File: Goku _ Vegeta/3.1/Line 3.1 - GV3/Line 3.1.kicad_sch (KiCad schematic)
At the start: 112 parts, among them J1 Solenoid, J10 RIGHT HEADERS, J11 Kicker Voltmeter, J3 Motor 1, J4 Motor 3, J5 Motor 2, J6 Motor 4, J7 BATTERY POWER, J8 I2C TO MASTER, J9 LEFT HEADERS, Q2 BSC040N10NS5, U1 LM2587S-ADJ, U10 TPS62132, U11 TPS62133, U2 TB67H420FTG Dual/Single Motor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, U3 TB67H420FTG Dual/Single Motor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, U4 TB67H420FTG Dual/Single Motor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, U5 TB67H420FTG Dual/Single Motor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, U7 NXV55UNR, U9 DEV-16771

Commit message: abt halfway done with line 3.0
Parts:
- removed J3: Motor 1, Connector_PinSocket_2.54mm:PinSocket_1x06_P2.54mm_Vertical, symbol Connector:Conn_01x06_Pin
- removed J4: Motor 3, Connector_PinSocket_2.54mm:PinSocket_1x06_P2.54mm_Vertical, symbol Connector:Conn_01x06_Pin
- removed J5: Motor 2, Connector_PinSocket_2.54mm:PinSocket_1x06_P2.54mm_Vertical, symbol Connector:Conn_01x06_Pin
- removed J6: Motor 4, Connector_PinSocket_2.54mm:PinSocket_1x06_P2.54mm_Vertical, symbol Connector:Conn_01x06_Pin
- removed U2, U3, U4, U5: TB67H420FTG Dual/Single Motor Driver Carrier, TB67H420FTG Dual_Single Motor Driver Carrier:TB67H420FTG DualSingle Motor Driver Carrier, symbol TB67H420FTG Dual_Single Motor Driver Carrier:LM2587S-ADJ
- added A17, A18, A19, A20, A21, A22, A23, A24, A25, A26, A27, A28, A29, A30, A31, A32, A33, A34, A35, A36: ALS-PT19-315C/L177/TR8, ALS-PT19-315C_L177_TR8:XDCR_ALS-PT19-315C_L177_TR8, symbol ALS-PT19-315C_L177_TR8:ALS-PT19-315C/L177/TR8
- added LED17, LED18, LED19, LED20, LED21, LED22, LED23, LED24, LED25, LED26, LED27, LED28, LED29, LED30, LED31, LED32, LED33, LED34, LED35, LED36: JB2835AWT-W-U30GA0000-N0000001, JB2835AWT-W-U30GA0000-N0000001:LED_J2835_CRW, symbol JB2835AWT-W-U30GA0000-N0000001:JB2835AWT-W-U30GA0000-N0000001
- added R40, R42, R44, R46, R48, R50, R52, R54, R56, R58, R60, R62, R64, R66, R68, R70, R72, R74, R76, R78: 12R, Resistor_SMD:R_0805_2012Metric, symbol Device:R_Small_US
- added R41, R43, R45, R47, R49, R51, R53, R55, R57, R59, R61, R63, R65, R67, R69, R71, R73, R75, R77, R79: 10K, Resistor_SMD:R_0805_2012Metric, symbol Device:R_Small_US
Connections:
- net SEN1 is gone; now on net 14: A1.2, A10.2, A11.2, A12.2, A13.2, A14.2, A15.2, A16.2, A2.2, A3.2, A4.2, A5.2, A6.2, A7.2, A8.2, A9.2, R10.2, R12.2, R14.2, R16.2, R18.2, R20.2, R22.2, R24.2, R26.2, R28.2, R33.2, R35.2, R37.2, R39.2, R5.2, R8.2
- net +3V3: now also A17.1, A18.1, A19.1, A20.1, A21.1, A22.1, A23.1, A24.1, A25.1, A26.1, A27.1, A28.1, A29.1, A30.1, A31.1, A32.1, A33.1, A34.1, A35.1, A36.1, R40.1, R42.1, R44.1, R46.1, R48.1, R50.1, R52.1, R54.1, R56.1, R58.1, R60.1, R62.1, R64.1, R66.1, R68.1, R70.1, R72.1, R74.1, R76.1, R78.1
- net 14: now also A17.2, A18.2, A19.2, A20.2, A21.2, A22.2, A23.2, A24.2, A25.2, A26.2, A27.2, A28.2, A29.2, A30.2, A31.2, A32.2, A33.2, A34.2, A35.2, A36.2, R41.2, R43.2, R45.2, R47.2, R49.2, R51.2, R53.2, R55.2, R57.2, R59.2, R61.2, R63.2, R65.2, R67.2, R69.2, R71.2, R73.2, R75.2, R77.2, R79.2; no longer J9.18 (Pin_18), U9.26 (A12)
- net 15: no longer J9.19 (Pin_19), U9.27 (A13)
- net GND: now also R41.1, R43.1, R45.1, R47.1, R49.1, R51.1, R53.1, R55.1, R57.1, R59.1, R61.1, R63.1, R65.1, R67.1, R69.1, R71.1, R73.1, R75.1, R77.1, R79.1
- net MSFTDRN: now also LED17.1, LED18.1, LED19.1, LED20.1, LED21.1, LED22.1, LED23.1, LED24.1, LED25.1, LED26.1, LED27.1, LED28.1, LED29.1, LED30.1, LED31.1, LED32.1, LED33.1, LED34.1, LED35.1, LED36.1
- new net: LED28.2, R62.2
- new net: LED31.2, R68.2
- new net: LED26.2, R58.2
- new net: LED24.2, R54.2
- new net: LED34.2, R74.2
- new net: LED22.2, R50.2
- new net: LED21.2, R48.2
- new net: LED18.2, R42.2
- new net: LED19.2, R44.2
- new net: LED32.2, R70.2
- new net: LED27.2, R60.2
- new net: LED17.2, R40.2
- new net: LED25.2, R56.2
- new net: LED20.2, R46.2
- new net: LED36.2, R78.2
- new net: LED33.2, R72.2
- new net: LED30.2, R66.2
- new net: LED23.2, R52.2
- new net: LED35.2, R76.2
- new net: LED29.2, R64.2
- new net 26: J9.18 (Pin_18), U9.26 (A12)
- new net 27: J9.19 (Pin_19), U9.27 (A13)
- no-connect marks 54 -> 14
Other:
- note added: "Cross line sensors - conditional poll 1"
- note added: "DONE 16 outer circle line sensors DONE 16 cross sensors DONE 8 inner cicle sensors DONE 36 line sensors in total maxon brushless motor controllers adapter board two cables connecting line and main pcb - power xt60 cable - idc data cable kicker charge pump no imu 36 leds using actual LED driver good power rails that are rated for 2 x of projected power draw"
- note added: "GOALS FOR LINE 3.1"
- note added: "Inner ring line sensors - conditional poll 2"
- note added: "Outer ring line sensors - constant poll"
- note added: "STILL GOTTA CHAT WITH KEVIN ABOUT LINE SENSOR ORENTATION - WE ARE NO ONLY DOES 16 LINE SENSORS IN TOTOAL THAT ALL ME HAVE GOT TO WORK WITH"
- note removed: "2nd Warning Line Sensors - Conditonal Poll"
- note removed: "Urgent Line Sensors - Conditional Poll"
- note removed: "Warning Line Sensors - Constant Poll"
- moved on the sheet: A1, A2, A3, A4, C1, C10, C15, C16, C17, C18, C2, C3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

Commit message: move to 3.1
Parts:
- removed A17, A18, A19, A20, A21, A22, A23, A24, A25, A26, A27, A28, A29, A30, A31, A32, A33, A34, A35, A36: ALS-PT19-315C/L177/TR8, ALS-PT19-315C_L177_TR8:XDCR_ALS-PT19-315C_L177_TR8, symbol ALS-PT19-315C_L177_TR8:ALS-PT19-315C/L177/TR8
- removed C1, C6: 100uF, Capacitor_THT:CP_Radial_D10.0mm_P5.00mm, symbol Device:C_Polarized_Small
- removed C10, C16: 0.1uF, Capacitor_SMD:C_0805_2012Metric, symbol Device:C_Polarized_Small
- removed C15, C8: 10uF, Capacitor_SMD:C_0805_2012Metric, symbol Device:C_Polarized_Small
- removed C17, C9: 3.3nF, Capacitor_SMD:C_0805_2012Metric, symbol Device:C_Polarized_Small
- removed C18, C7: 22uF, Capacitor_SMD:C_0805_2012Metric, symbol Device:C_Polarized_Small
- removed C2, C5: 1uF, Capacitor_SMD:C_0805_2012Metric, symbol Device:C_Polarized_Small
- removed C3, C4: 560uF, Capacitor_THT:CP_Radial_D18.0mm_P7.50mm, symbol Device:C_Polarized
- removed D1: SS510, Diode_SMD:D_SOD-128, symbol Device:D_Schottky
- removed D2, D3, D5: STTH2002G-TR, Package_TO_SOT_SMD:TO-263-2, symbol Diode:STTH2002G
- removed J1: Solenoid, TerminalBlock:TerminalBlock_bornier-2_P5.08mm, symbol Connector:Screw_Terminal_01x02
- removed J11: Kicker Voltmeter, TerminalBlock:TerminalBlock_bornier-2_P5.08mm, symbol Connector:Screw_Terminal_01x02
- removed J7: BATTERY POWER, Connector_AMASS:AMASS_XT60-F_1x02_P7.20mm_Vertical, symbol Connector:Conn_01x02_Male
- removed J8: I2C TO MASTER, Connector_JST:JST_XH_B4B-XH-AM_1x04_P2.50mm_Vertical, symbol Connector:Conn_01x04_Male
- removed L1: 56uH, Inductor_SMD:L_Bourns_SRR1260, symbol Device:L
- removed L2, L3: 2.2uH, Inductor_SMD:L_Bourns_SRR1260, symbol Device:L
- removed LED17, LED18, LED19, LED20, LED21, LED22, LED23, LED24, LED25, LED26, LED27, LED28, LED29, LED30, LED31, LED32, LED33, LED34, LED35, LED36: JB2835AWT-W-U30GA0000-N0000001, JB2835AWT-W-U30GA0000-N0000001:LED_J2835_CRW, symbol JB2835AWT-W-U30GA0000-N0000001:JB2835AWT-W-U30GA0000-N0000001
- removed Q2: BSC040N10NS5, Package_TO_SOT_SMD:TDSON-8-1, symbol Transistor_FET:BSC040N10NS5
- removed R1: 2K94, Resistor_SMD:R_0805_2012Metric, symbol Device:R_Small
- removed R2: 57K, Resistor_SMD:R_0805_2012Metric, symbol Device:R_Small
- removed R29: CT6EP103, POT_CT-6EP_NDC:POT_CT-6EP_NDC, symbol POT_CT-6EP_NDC:CT6EP103
- removed R3: 1K5, Resistor_SMD:R_0805_2012Metric, symbol Device:R_Small
- removed R30, R32: 100K, Resistor_SMD:R_0805_2012Metric, symbol Device:R_Small
- removed R33, R35, R37, R39, R41, R43, R45, R47, R49, R51, R53, R55, R57, R59, R61, R63, R65, R67, R69, R71, R73, R75, R77, R79: 10K, Resistor_SMD:R_0805_2012Metric, symbol Device:R_Small_US
- removed R34, R36, R38, R40, R42, R44, R46, R48, R50, R52, R54, R56, R58, R60, R62, R64, R66, R68, R70, R72, R74, R76, R78, R9: 12R, Resistor_SMD:R_0805_2012Metric, symbol Device:R_Small_US
- removed R7: 10K, Resistor_SMD:R_0805_2012Metric, symbol Device:R_Small
- removed U1: LM2587S-ADJ, LM2587S-ADJ:VREG_TPS79625KTTR, symbol LM2587S-ADJ:LM2587S-ADJ
- removed U10: TPS62132, Package_DFN_QFN:VQFN-16-1EP_3x3mm_P0.5mm_EP1.68x1.68mm_ThermalVias, symbol Regulator_Switching:TPS62132
- removed U11: TPS62133, Package_DFN_QFN:VQFN-16-1EP_3x3mm_P0.5mm_EP1.68x1.68mm_ThermalVias, symbol Regulator_Switching:TPS62133
- removed U7: NXV55UNR, NXV55UNR:TRANS_BC846B,215, symbol NXV55UNR:NXV55UNR
- added J13: MID HEADERS, Connector_PinHeader_2.54mm:PinHeader_1x05_P2.54mm_Vertical, symbol Connector:Conn_01x05_Socket
- added J2: BACKUP 5V, Connector_AMASS:AMASS_XT30U-F_1x02_P5.0mm_Vertical, symbol Connector:Conn_01x02_Male
- added J4: I2C, Connector_AMASS:AMASS_XT30U-F_1x02_P5.0mm_Vertical, symbol Connector:Conn_01x02_Male
- added R2, R3, R4, R5, R7: 36R, Resistor_SMD:R_0805_2012Metric, symbol Device:R_Small_US
- added R29, R30, R32: 10K, Resistor_SMD:R_0805_2012Metric, symbol Device:R_Small_US
- R1: renamed from R4; value 12R -> 36R
- R11, R13, R15, R25, R27, R31: value 12R -> 10K
- R17, R19, R21, R23, R6: value 12R -> 36R
- R18, R20, R22, R24, R8: value 10K -> 36R
- renumbered J9 to J11, J10 to J12, R5 to R9, U9 to U8
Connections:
- net MSFTDRN is gone; now on net GND: LED1.1, LED10.1, LED11.1, LED12.1, LED13.1, LED14.1, LED15.1, LED16.1, LED2.1, LED3.1, LED4.1, LED5.1, LED6.1, LED7.1, LED8.1, LED9.1
- net +5V: now also A1.1, A10.1, A11.1, A12.1, A13.1, A14.1, A15.1, A16.1, A2.1, A3.1, A4.1, A5.1, A6.1, A7.1, A8.1, A9.1, R1.1, R17.1, R18.1, R19.1, R20.1, R21.1, R22.1, R23.1, R24.1, R6.1, R8.1, J2.2 (Pin_2), R2.1, R3.1, R4.1, R5.1, R7.1; no longer J12.1 (Pin_1)
- net 14: now also R30.2; no longer A1.2, A10.2, A11.2, A12.2, A13.2, A15.2, A16.2, A2.2, A3.2, A4.2, A5.2, A6.2, A7.2, A8.2, A9.2, R10.2, R12.2, R14.2, R16.2, R18.2, R20.2, R22.2, R24.2, R26.2, R28.2, R8.2, R9.2
- net 15: now also A15.2, R31.2
- net 16: now also A16.2, R32.2
- net 17: now also A9.2, R25.2
- net 18: now also J4.2 (Pin_2)
- net 19: now also J4.1 (Pin_1)
- net 20: now also A5.2, R13.2
- net 21: now also A1.2, R9.2
- net 22: now also A8.2, R16.2
- net 23: now also A4.2, R12.2
- net 24: now also A3.2, R11.2
- net 25: now also A7.2, R15.2
- net 26: now also A2.2, R10.2
- net 27: now also A6.2, R14.2
- net 38: now also A10.2, R26.2
- net 39: now also A11.2, R27.2
- net 40: now also A12.2, R28.2
- net 41: now also A13.2, R29.2
- net GND: now also R11.1, R13.1, R15.1, R25.1, R27.1, R31.1, J13.3 (Pin_3), J2.1 (Pin_1), R29.1, R30.1, R32.1; no longer R18.1, R20.1, R22.1, R24.1, R8.1
- net at LED3.2: now also R3.2
- net at LED8.2: now also R8.2; no longer R19.2
- net at LED16.2: now also R24.2
- net at LED12.2: now also R20.2; no longer R27.2
- net at LED4.2: now also R4.2; no longer R11.2
- net at LED6.2: now also R6.2; no longer R15.2
- net at LED15.2: now also R23.2
- net at LED10.2: now also R18.2; no longer R23.2
- net at R17.2: now also LED9.2; no longer LED7.2
- net at LED14.2: now also R22.2
- net at LED11.2: now also R19.2; no longer R25.2
- net at LED13.2: now also R21.2; no longer R31.2
- net at LED5.2: now also R5.2; no longer R13.2
- net ON/OFF: now reaches U8.ON/OFF
- net ON/OFF: now also J13.1 (Pin_1)
- net PROGRAM: now reaches U8.PROGRAM
- net PROGRAM: now also J13.2 (Pin_2)
- net at LED2.2: now also R2.2; no longer R6.2
- removed net +3V3: A1.1, A10.1, A11.1, A12.1, A13.1, A14.1, A15.1, A16.1, A2.1, A3.1, A4.1, A5.1, A6.1, A7.1, A8.1, A9.1, J11.15 (Pin_15), J12.3 (Pin_3), R1.1, R11.1, R13.1, R15.1, R17.1, R19.1, R21.1, R23.1, R25.1, R27.1, R31.1, R6.1
- new net: LED7.2, R7.2
- no-connect marks 14 -> 17
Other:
- note added: "2nd Warning Line Sensors - Conditional Poll"
- note added: "NEXT STEPS: MAYBE: add spi bus"
- note added: "Warning Line Sensors - Constant Poll"
- note removed: "3V3 POWER RAIL - LEDs and Phototransistors"
- note removed: "5V POWER RAIL - Microcontroller"
- note removed: "Boost Circuit"
- note removed: "Cross line sensors - conditional poll 1"
- note removed: "DONE 16 outer circle line sensors DONE 16 cross sensors DONE 8 inner cicle sensors DONE 36 line sensors in total maxon brushless motor controllers adapter board two cables connecting line and main pcb - power xt60 cable - idc data cable kicker charge pump no imu 36 leds using actual LED driver good power rails that are rated for 2 x of projected power draw"
- note removed: "GOALS FOR LINE 3.1"
- note removed: "Inner ring line sensors - conditional poll 2"
- note removed: "KICKER CHARGE PUMP"
- note removed: "Kick Circuit"
- note removed: "LEDs Dimming"
- note removed: "MOTOR DRIVERS"
- note removed: "NEXT STEPS: add footprint for motor drivers finish adding in footprints for inductors etc. MAYBE:"
- note removed: "Outer ring line sensors - constant poll"
- note removed: "POWER SUPPLY"
- note removed: "STILL GOTTA CHAT WITH KEVIN ABOUT LINE SENSOR ORENTATION - WE ARE NO ONLY DOES 16 LINE SENSORS IN TOTOAL THAT ALL ME HAVE GOT TO WORK WITH"
- moved on the sheet: A1, J11, J12, LED1, R1, R9, U8

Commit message: MAIN 3.1 DONE no silkscreen
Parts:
- added C1, C2: 10uF, Capacitor_SMD:C_0805_2012Metric, symbol Device:C_Small
- added U1: ~, Converter_DCDC:Pololu 3.3V, 500mA Step-Down Voltage Regulator D24V5F3, symbol Converter_DCDC:Pololu_3.3V,_500mA_Step-Down_Voltage_Regulator_D24V5F3_
- J11, J12: footprint Connector_PinHeader_2.54mm:PinHeader_1x24_P2.54mm_Vertical -> Connector_PinSocket_2.54mm:PinSocket_1x24_P2.54mm_Vertical
- J13: footprint Connector_PinHeader_2.54mm:PinHeader_1x05_P2.54mm_Vertical -> Connector_PinSocket_2.54mm:PinSocket_1x05_P2.54mm_Vertical
- J2: value BACKUP 5V -> 5V LINE
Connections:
- net +5V: now also J12.1 (Pin_1), C2.1, U1.2 (VIN); no longer A1.1, A10.1, A11.1, A12.1, A13.1, A14.1, A15.1, A16.1, A2.1, A3.1, A4.1, A5.1, A6.1, A7.1, A8.1, A9.1
- net GND: now also C1.2, C2.2, U1.3 (GND)
- new net +3V3: A1.1, A10.1, A11.1, A12.1, A13.1, A14.1, A15.1, A16.1, A2.1, A3.1, A4.1, A5.1, A6.1, A7.1, A8.1, A9.1, C1.1, U1.4 (VOUT)

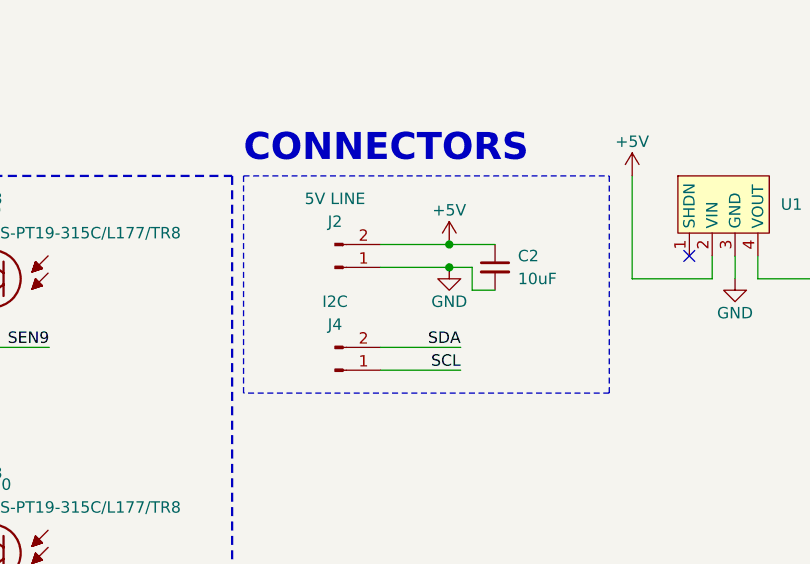
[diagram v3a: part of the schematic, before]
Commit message: Main and Line 3.1 done w/ silkscreen
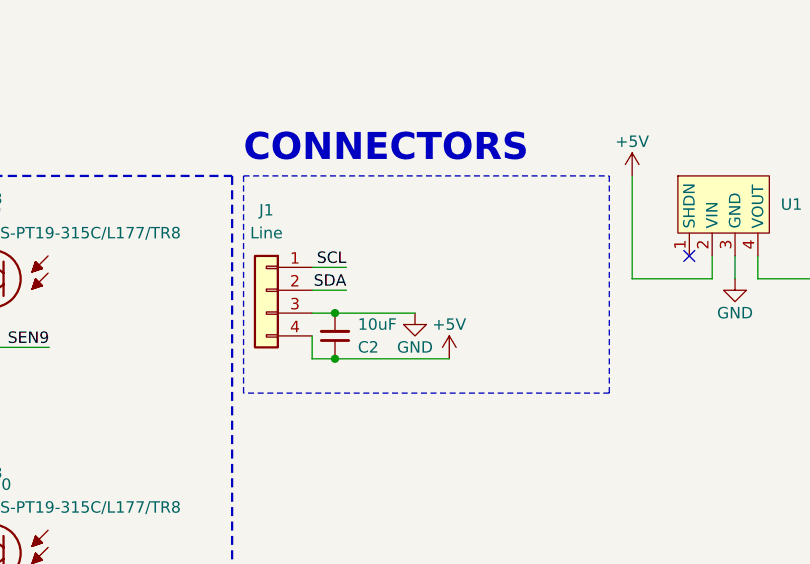
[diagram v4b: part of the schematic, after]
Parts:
- removed J2: 5V LINE, Connector_AMASS:AMASS_XT30U-F_1x02_P5.0mm_Vertical, symbol Connector:Conn_01x02_Male
- removed J4: I2C, Connector_AMASS:AMASS_XT30U-F_1x02_P5.0mm_Vertical, symbol Connector:Conn_01x02_Male
- added J1: Line, Connector_JST:JST_XH_B4B-XH-A_1x04_P2.50mm_Vertical, symbol Connector_Generic:Conn_01x04
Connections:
- net +5V: now also J1.4 (Pin_4)
- net 18: now also J1.2 (Pin_2)
- net 19: now also J1.1 (Pin_1)
- net GND: now also J1.3 (Pin_3)
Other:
- moved on the sheet: C2
